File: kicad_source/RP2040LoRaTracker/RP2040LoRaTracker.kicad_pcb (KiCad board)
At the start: 2 copper layers, 28 x 87 mm, 69 parts, among them J1 USB_B_Micro, J2 BM04B-SRSS-TB, Q1 NTR4171P, SW1 SW_Push, SW2 SW_Push, SW3 SW_SPDT, U1 RP2040, U2 Ai-Thinker-Ra-01, U3 NEO-M8N, U4 W25Q16JVSS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

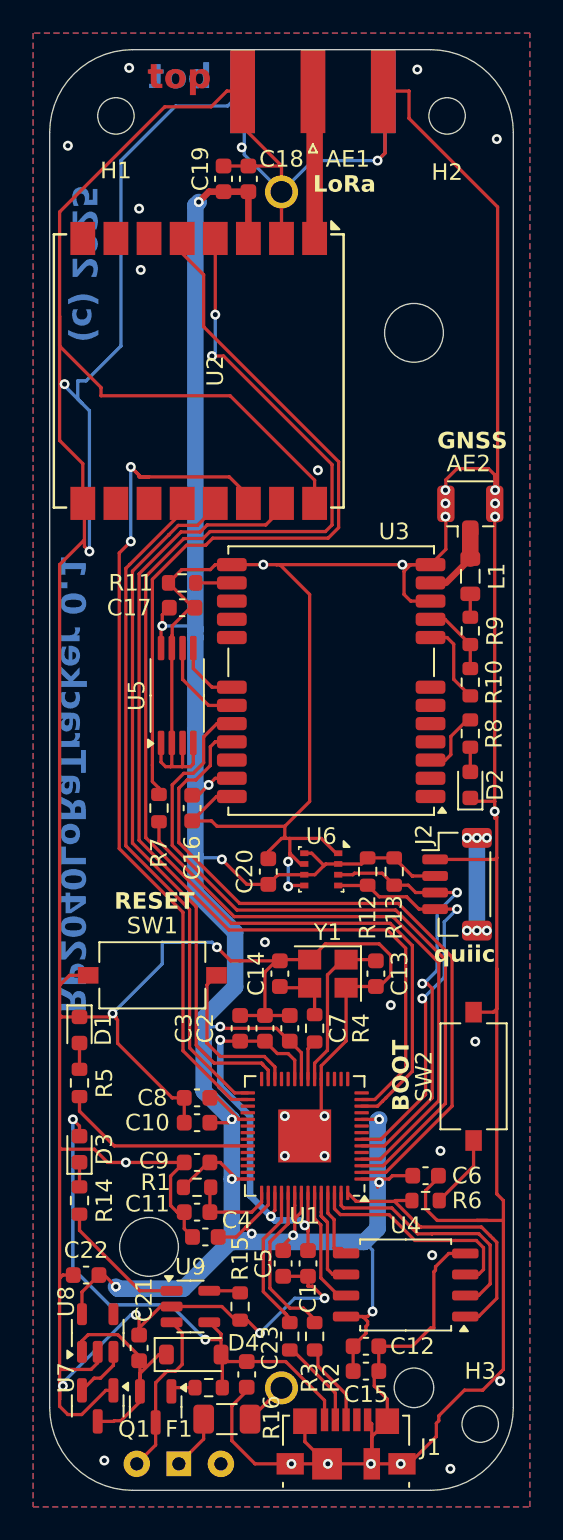
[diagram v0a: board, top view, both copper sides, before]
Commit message: added battery voltage measurement, R17 and R18
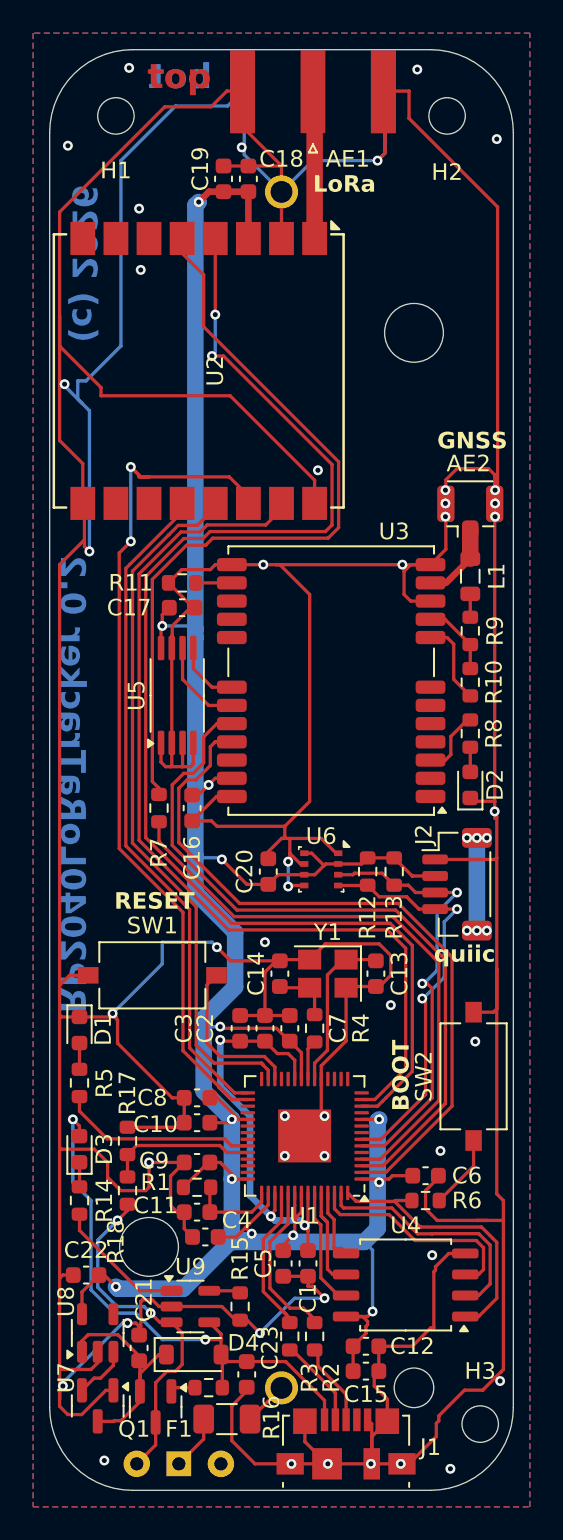
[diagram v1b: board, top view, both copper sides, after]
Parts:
- added R17: 110k, Resistor_SMD:R_0603_1608Metric, F.Cu at (129.7, 119.9)
- added R18: 220k, Resistor_SMD:R_0603_1608Metric, F.Cu at (129.7, 122.9)
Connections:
- U1 pad 38: unconnected-(U1-GPIO26_ADC0-Pad38) -> /RP2040/MEASURE_BATT
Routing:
- net +BATT: track 10.2 -> 21.3 mm, vias 0 -> 2
- net /RP2040/MEASURE_BATT: track 0.00 -> 9.02 mm
- net GND: track 520.0 -> 526.9 mm
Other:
- board text added: "(c) 2026"
- board text added: "RP2040LoRaTracker 0.2"
- board text removed: "(c) 2025"
- board text removed: "RP2040LoRaTracker 0.1"

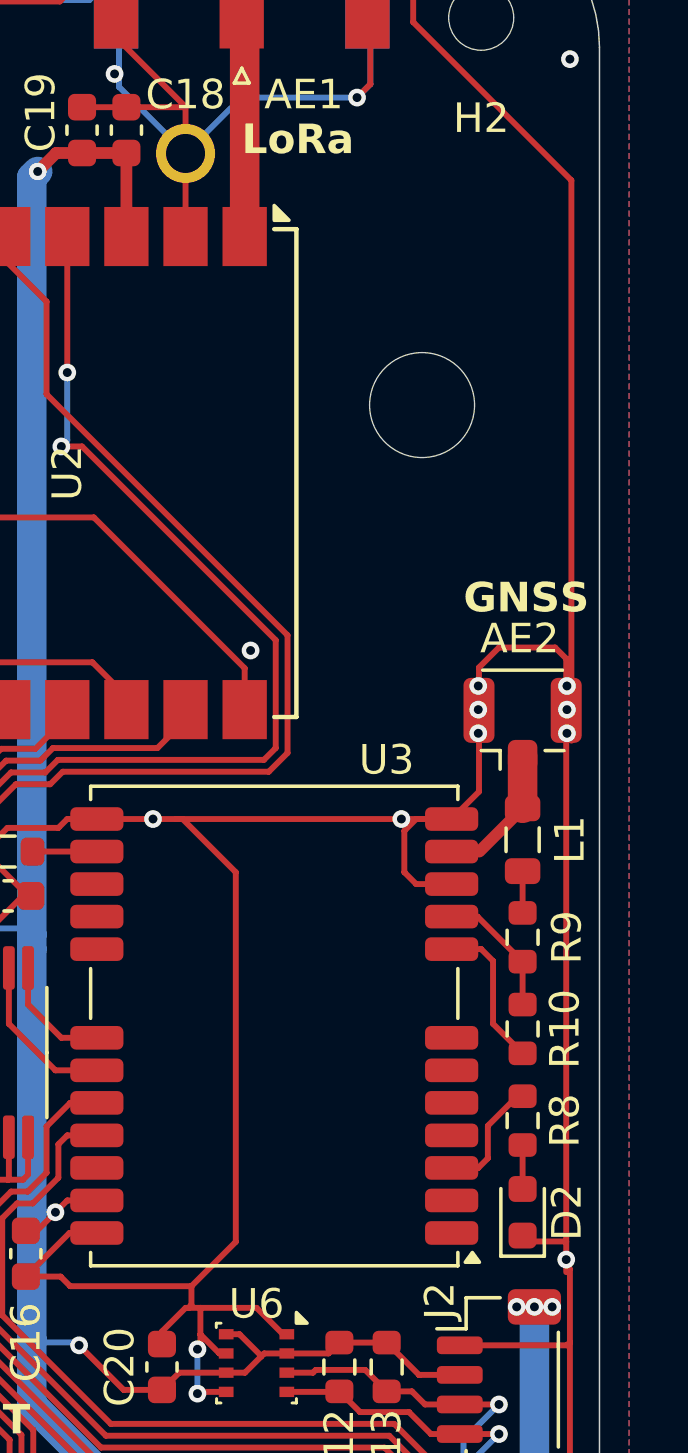
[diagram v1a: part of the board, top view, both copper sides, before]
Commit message: added battery voltage measurement, R17 and R18
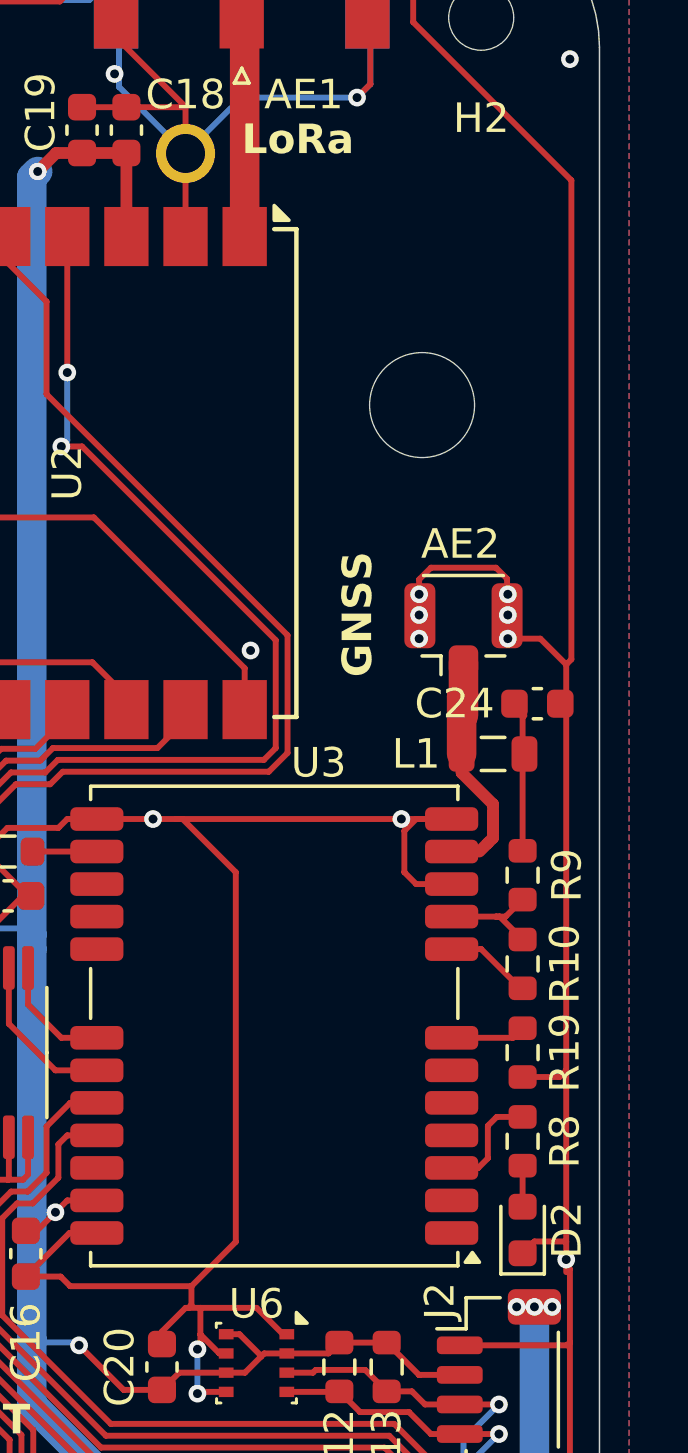
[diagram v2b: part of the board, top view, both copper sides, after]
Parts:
- added C24: 100 nF, Capacitor_SMD:C_0603_1608Metric, F.Cu at (150.9, 81.2)
- added R19: 0R, Resistor_SMD:R_0603_1608Metric, F.Cu at (150.4, 93.0)
- D1: value LED_Small -> LED_Small green
- D2: value LED_Small -> LED_Small blue
- D3: value LED_Small -> LED_Small red
- L1: value L -> 27 nH
- R9: value 1k -> 10R
- moved AE2 3.77 mm to (148.4, 78.7)
- moved L1 3.07 mm to (149.4, 82.9), turned to 180 degrees
- moved R10 2.20 mm to (150.4, 90.0)
- moved R9 2.10 mm to (150.4, 87.0)
- moved R8 0.70 mm to (150.4, 96.0)
- moved D2 0.60 mm to (150.4, 99.0)
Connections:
- net Net-(L1-Pad1) renamed /LoRa GNSS/VCC_RF_R
- U3 pad 7: unconnected-(U3-VDD_USB-Pad7) -> /LoRa GNSS/VDD_USB
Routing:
- net /LoRa GNSS/NEO_ANTENNA: track 4.79 -> 10.4 mm
- net /LoRa GNSS/VCC_RF_R: track 1.41 -> 4.95 mm
- net /LoRa GNSS/VDD_USB: track 0.00 -> 2.53 mm
- net /LoRa GNSS/NEO_RESET: track 5.10 -> 2.95 mm
- net /LoRa GNSS/VCC_RF: track 4.48 -> 3.86 mm
